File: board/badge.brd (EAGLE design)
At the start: 55.6 x 67.5 mm, 46 parts, among them IC1 STM32F030F4, IC2 UBLOX_MAX, IC3 RFM69HW, IC4 MCP1640, J2 20-0096, J3 SWD_PTH_SHROUD, X1 RADIOMETRIX-MTX2, X2 SMA-142-0701-851/861, X3 091OLED

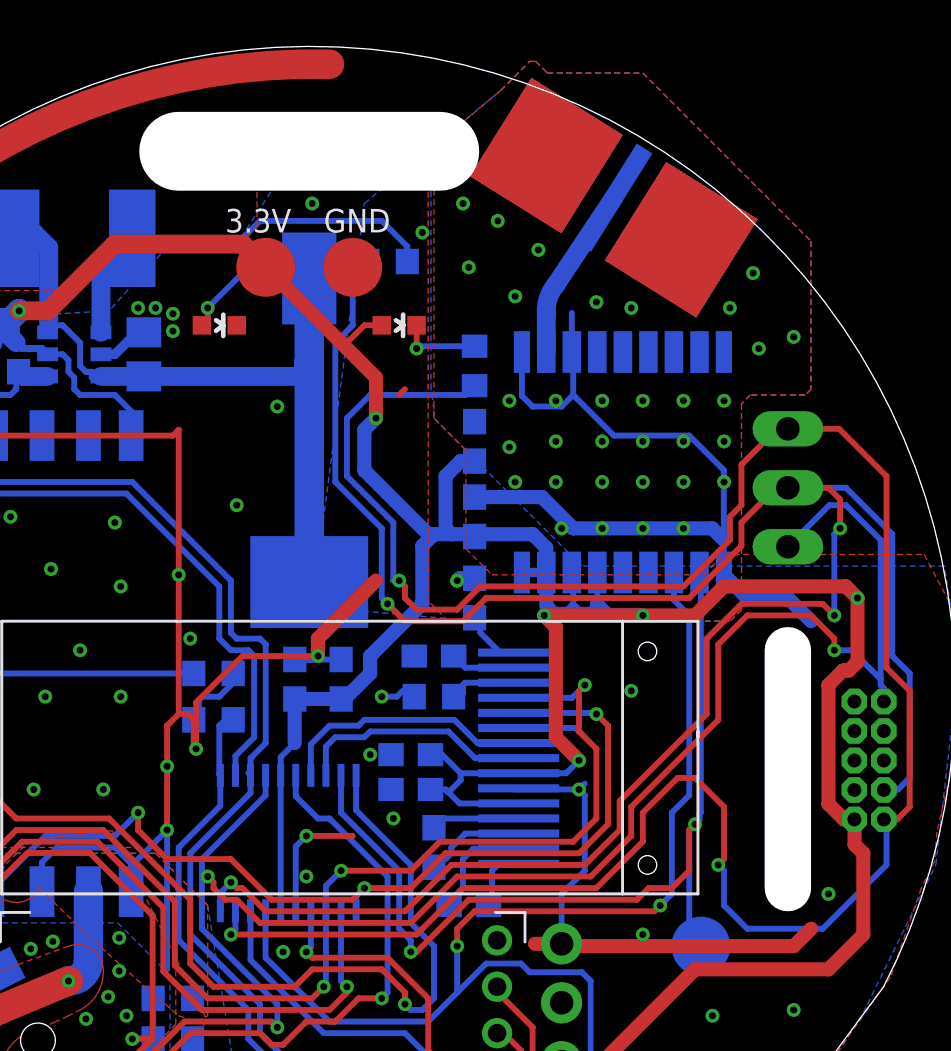
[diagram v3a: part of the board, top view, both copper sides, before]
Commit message: Amended milling layer
Made them dimension layer instead. Confuses the fab by 87.2% less.
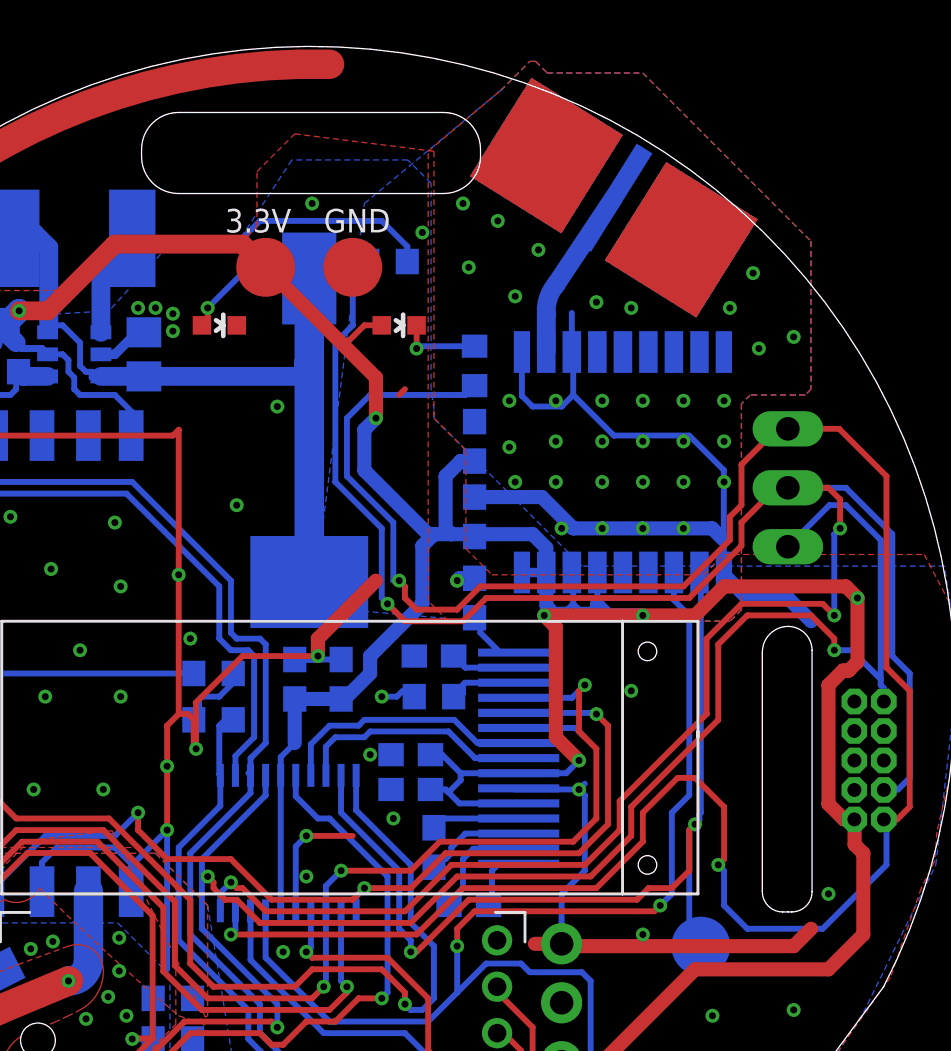
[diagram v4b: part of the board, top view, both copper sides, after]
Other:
- outline, holes or cut-outs redrawn
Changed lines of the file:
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@@
 <setting verticaltext="up"/>
 </settings>
-<grid distance="0.25" unitdist="mm" unit="mm" style="lines" multiple="1" display="no" altdistance="0.125" altunitdist="mm" altunit="mm"/>
+<grid distance="0.079375" unitdist="mm" unit="mm" style="lines" multiple="1" display="yes" altdistance="0.125" altunitdist="mm" altunit="mm"/>
 <layers>
 <layer number="1" name="Top" color="4" fill="1" visible="yes" active="yes"/>
@@
 <layer number="220" name="220bmp" color="21" fill="1" visible="no" active="no"/>
 <layer number="221" name="221bmp" color="22" fill="1" visible="no" active="no"/>
-<layer number="222" name="222bmp" color="23" fill="1" visible="no" active="no"/>
 <layer number="223" name="223bmp" color="24" fill="1" visible="no" active="no"/>
 <layer number="224" name="224bmp" color="25" fill="1" visible="no" active="no"/>
@@
 <text x="48" y="33.5" size="1.016" layer="22" font="vector" ratio="14" rot="SMR90">3.3V only</text>
 <text x="47.5" y="42.75" size="1.016" layer="22" font="vector" ratio="14" rot="MR270">Remove battery</text>
-<wire x1="53.25" y1="55.25" x2="53.25" y2="45" width="2" layer="46"/>
 <text x="54.75" y="60.25" size="1.016" layer="22" font="vector" ratio="13" rot="MR180">RST</text>
 <text x="54.75" y="62.75" size="1.016" layer="22" font="vector" ratio="13" rot="MR180">CLK</text>
@@
 <text x="55" y="66.75" size="1.27" layer="22" font="vector" ratio="13" rot="MR0">SWD</text>
 <text x="58.25" y="45.75" size="1.27" layer="22" font="vector" ratio="13" rot="MR0">SWD</text>
-<wire x1="27" y1="76.75" x2="38.25" y2="76.75" width="3.4" layer="46"/>
 <text x="25" y="22.5" size="1.27" layer="21" font="vector" ratio="13" rot="R90">RESET</text>
 <text x="41.75" y="23" size="1.27" layer="21" font="vector" ratio="13" rot="R90">BOOT</text>
@@
 <wire x1="32.625" y1="12.75" x2="32.625" y2="85.375" width="0" layer="51" style="longdash"/>
 <text x="40" y="17.25" size="1.016" layer="21" font="vector" ratio="14" rot="R56">Rev. A May '14</text>
+<wire x1="26.9875" y1="78.4225" x2="38.4175" y2="78.4225" width="0" layer="20"/>
+<wire x1="38.4175" y1="78.4225" x2="40.005" y2="76.835" width="0" layer="20" curve="-90"/>
+<wire x1="40.005" y1="76.835" x2="40.005" y2="76.5175" width="0" layer="20"/>
+<wire x1="40.005" y1="76.5175" x2="38.4175" y2="74.93" width="0" layer="20" curve="-90"/>
+<wire x1="38.4175" y1="74.93" x2="26.9875" y2="74.93" width="0" layer="20"/>
+<wire x1="26.9875" y1="74.93" x2="25.4" y2="76.5175" width="0" layer="20" curve="-90"/>
+<wire x1="25.4" y1="76.5175" x2="25.4" y2="76.835" width="0" layer="20"/>
+<wire x1="25.4" y1="76.835" x2="26.9875" y2="78.4225" width="0" layer="20" curve="-90"/>
+<wire x1="53.260625" y1="56.276875" x2="54.2925" y2="55.245" width="0" layer="20" curve="-90"/>
+<wire x1="54.2925" y1="55.245" x2="54.2925" y2="44.846875" width="0" layer="20"/>
+<wire x1="54.2925" y1="44.846875" x2="53.419375" y2="43.97375" width="0" layer="20" curve="-90"/>
+<wire x1="53.419375" y1="43.97375" x2="53.260625" y2="43.97375" width="0" layer="20"/>
+<wire x1="53.260625" y1="43.97375" x2="53.0225" y2="43.97375" width="0" layer="20"/>
+<wire x1="53.0225" y1="43.97375" x2="52.149375" y2="44.846875" width="0" layer="20" curve="-90"/>
+<wire x1="52.149375" y1="44.846875" x2="52.149375" y2="55.165625" width="0" layer="20"/>
+<wire x1="52.149375" y1="55.165625" x2="53.260625" y2="56.276875" width="0" layer="20" curve="-90"/>
 </plain>
 <attributes>
@@
 </signal>
 </signals>
-<errors>
-</errors>
 </board>
 </drawing>

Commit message: started rev2
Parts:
- added C13, C14: 1u, rcl:C0603
- added R10: 220k, rcl:R0603
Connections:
- removed net O_RES: IC1.7, X3.9
- new net N$22: C13.2, R10.1, X3.9
- new net N$23: C14.2, J2.4_1, J2.4_2
- new net O_DC: IC1.7, X3.10
- net +3V3: now also R10.2
- net 0V: now also C13.1; no longer X3.10
- net ADC1: now also C14.1; no longer J2.4_1, J2.4_2
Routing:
- net N$22: track 0.00 -> 25.5 mm, vias 0 -> 2
- net O_RES: track 11.1 -> 0.00 mm
- net O_DC: track 0.00 -> 10.9 mm
- net N$9: track 20.6 -> 14.2 mm
- net +3V3: track 217.3 -> 223.1 mm, vias 10 -> 11
- net CS: track 46.0 -> 43.1 mm
- net 0V: track 222.4 -> 220.6 mm, vias 115 -> 121
- net ADC1: track 54.0 -> 52.5 mm
- net N$18: track 43.2 -> 44.5 mm
- net SCK: track 41.0 -> 41.6 mm
- net MOSI: track 54.0 -> 54.6 mm
- net TX: track 13.7 -> 14.3 mm
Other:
- outline, holes or cut-outs redrawn

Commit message: rev2 almost done
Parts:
- added R11: 10k, rcl:R0603
- moved C14 1.67 mm to (26.8, 35.0)
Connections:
- new net N$24: C14.1, R11.2
- net ADC1: now also R11.1; no longer C14.1
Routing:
- net 0V: track 220.6 -> 191.6 mm, vias 121 -> 131
- net N$23: track 0.00 -> 26.6 mm, vias 0 -> 2
- net ADC1: track 52.5 -> 29.0 mm, vias 5 -> 2
- net N$9: track 14.2 -> 21.8 mm, vias 0 -> 2
- net N$19: track 14.2 -> 11.2 mm
- net N$18: track 44.5 -> 42.1 mm
- net N$24: track 0.00 -> 1.75 mm
- net N$8: track 52.5 -> 51.5 mm
- net TX_EN: track 62.1 -> 62.6 mm
- net +3V3: track 223.1 -> 223.6 mm

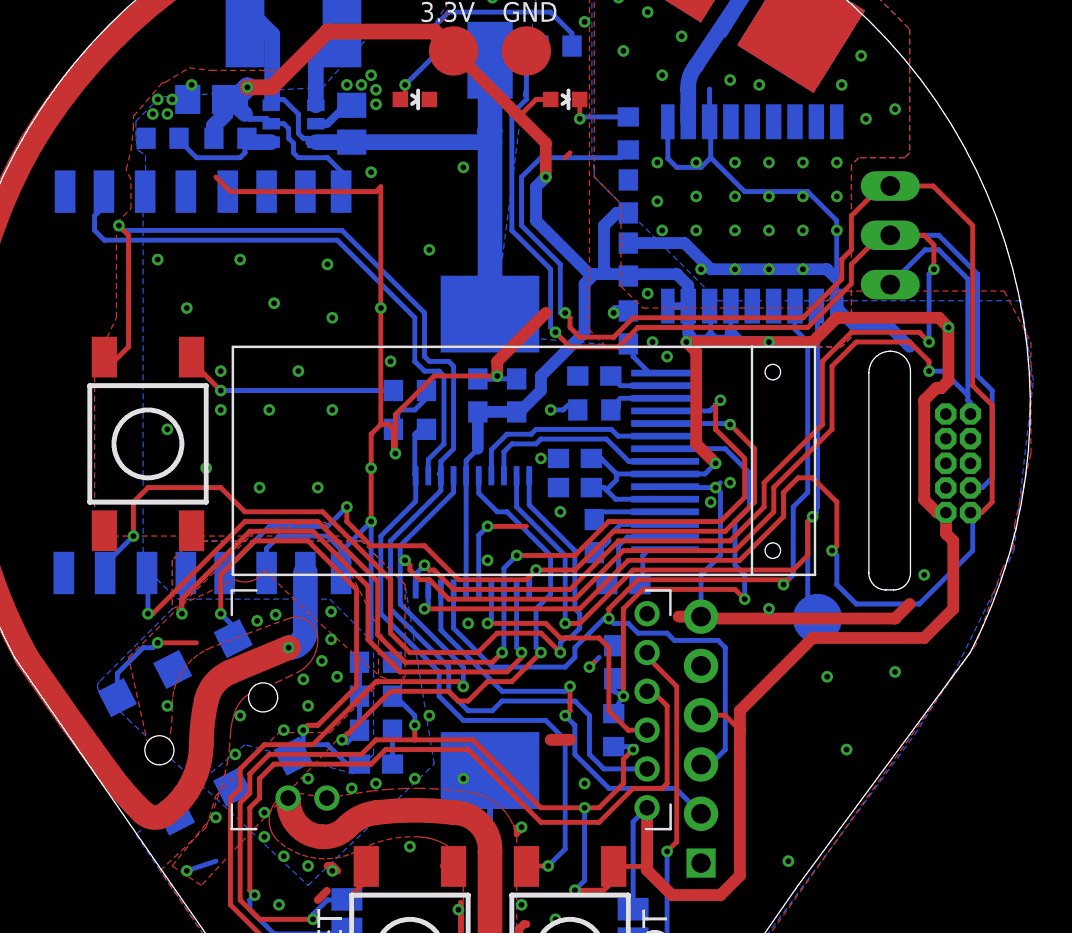
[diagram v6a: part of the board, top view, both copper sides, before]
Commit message: switching tx/rx on ftdi
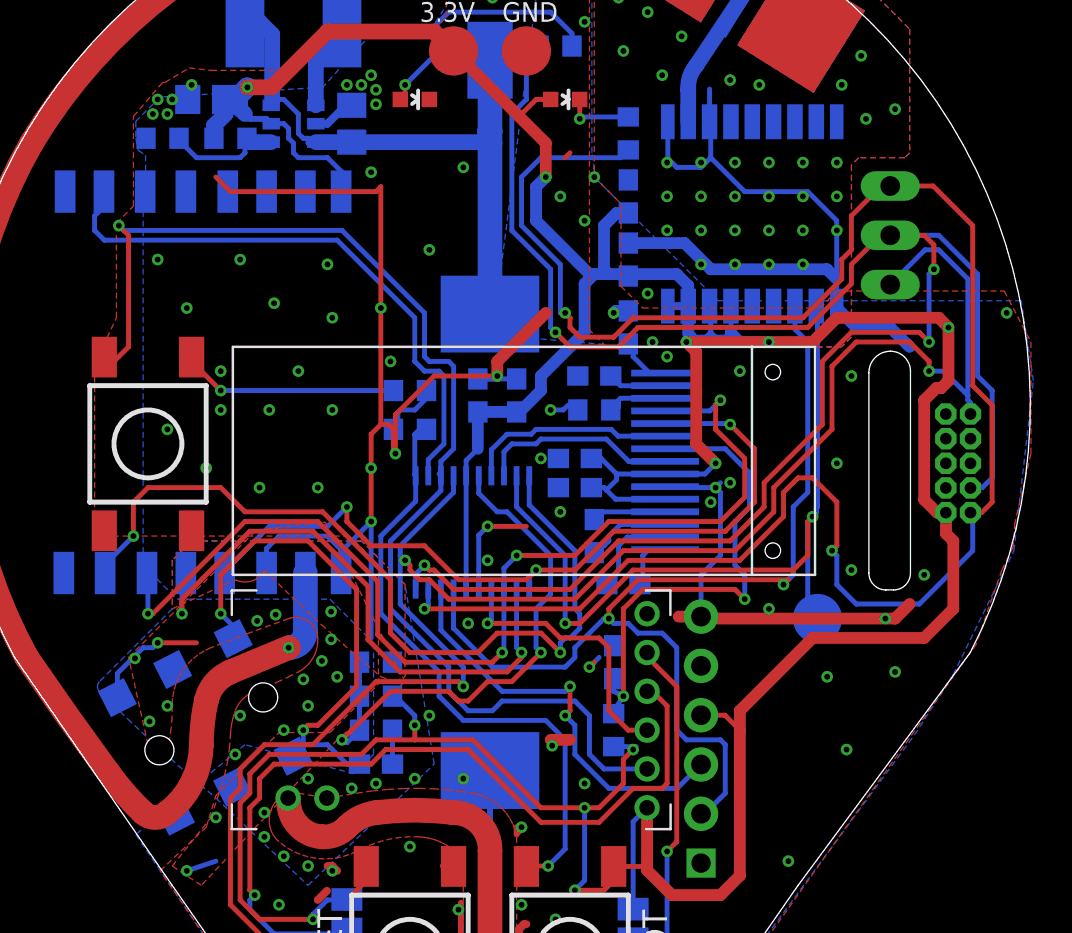
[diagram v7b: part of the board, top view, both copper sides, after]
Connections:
- net N$8: now also JP1.P$2; no longer JP1.P$3
- net N$9: now also JP1.P$3; no longer JP1.P$2
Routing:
- net N$8: track 51.5 -> 53.4 mm
- net 0V: vias 131 -> 143
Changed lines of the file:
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@@
 <setting verticaltext="up"/>
 </settings>
-<grid distance="9.84251969" unitdist="mil" unit="mil" style="lines" multiple="1" display="yes" altdistance="0.125" altunitdist="mm" altunit="mm"/>
+<grid distance="0.25" unitdist="mm" unit="mm" style="lines" multiple="1" display="yes" altdistance="0.125" altunitdist="mm" altunit="mm"/>
 <layers>
 <layer number="1" name="Top" color="4" fill="1" visible="yes" active="yes"/>
@@
 <vertex x="13.375" y="58"/>
 <vertex x="13.375" y="62.875"/>
-<vertex x="14.125" y="63.625"/>
-<vertex x="14.125" y="65.125"/>
-<vertex x="13.875" y="65.625"/>
-<vertex x="14.125" y="66.625"/>
-<vertex x="14.25" y="67.75"/>
+<vertex x="14.25" y="63.75"/>
 <vertex x="14.25" y="68.375"/>
 <vertex x="15.75" y="70.125"/>
@@
 <vertex x="40.99" y="17.72625"/>
 </polygon>
-<via x="48.75" y="60.5" extent="1-16" drill="0.3"/>
+<via x="48.75" y="60.75" extent="1-16" drill="0.3"/>
 <via x="48.75" y="64.25" extent="1-16" drill="0.3"/>
-<via x="47" y="60.5" extent="1-16" drill="0.3"/>
+<via x="47" y="60.75" extent="1-16" drill="0.3"/>
 <via x="47" y="62.5" extent="1-16" drill="0.3"/>
 <via x="47" y="64.25" extent="1-16" drill="0.3"/>
 <via x="47" y="66" extent="1-16" drill="0.3"/>
-<via x="45.25" y="60.5" extent="1-16" drill="0.3"/>
+<via x="45.25" y="60.75" extent="1-16" drill="0.3"/>
 <via x="48.75" y="66" extent="1-16" drill="0.3"/>
 <via x="50.5" y="66" extent="1-16" drill="0.3"/>
@@
 <via x="45.25" y="64.25" extent="1-16" drill="0.3"/>
 <via x="45.25" y="66" extent="1-16" drill="0.3"/>
-<via x="43.25" y="62.5" extent="1-16" drill="0.3"/>
-<via x="43.25" y="64.25" extent="1-16" drill="0.3"/>
-<via x="43.25" y="66" extent="1-16" drill="0.3"/>
-<via x="41.25" y="66" extent="1-16" drill="0.3"/>
-<via x="41.25" y="64" extent="1-16" drill="0.3"/>
-<via x="41.5" y="62.5" extent="1-16" drill="0.3"/>
-<via x="43.5" y="60.5" extent="1-16" drill="0.3"/>
+<via x="43.5" y="62.5" extent="1-16" drill="0.3"/>
+<via x="43.5" y="64.25" extent="1-16" drill="0.3"/>
+<via x="43.5" y="66" extent="1-16" drill="0.3"/>
+<via x="41.75" y="66" extent="1-16" drill="0.3"/>
+<via x="41.75" y="64.25" extent="1-16" drill="0.3"/>
+<via x="41.75" y="62.5" extent="1-16" drill="0.3"/>
+<via x="43.5" y="60.75" extent="1-16" drill="0.3"/>
 <via x="51.75" y="71.5" extent="1-16" drill="0.3"/>
 <via x="50.75" y="70" extent="1-16" drill="0.3"/>
@@
 <via x="19.5" y="25.75" extent="1-16" drill="0.3"/>
 <via x="21" y="32.5" extent="1-16" drill="0.3"/>
+<via x="14.32875" y="40.44875" extent="1-16" drill="0.3"/>
+<via x="15.07875" y="37.19875" extent="1-16" drill="0.3"/>
+<via x="35.82875" y="35.94875" extent="1-16" drill="0.3"/>
+<via x="45.5" y="55.25" extent="1-16" drill="0.3"/>
+<via x="51.25" y="55" extent="1-16" drill="0.3"/>
+<via x="50.5" y="50.5" extent="1-16" drill="0.3"/>
+<via x="51.25" y="45" extent="1-16" drill="0.3"/>
+<via x="53" y="42.5" extent="1-16" drill="0.3"/>
+<via x="59.25" y="58.25" extent="1-16" drill="0.3"/>
+<via x="38" y="65.25" extent="1-16" drill="0.3"/>
+<via x="37.5" y="63" extent="1-16" drill="0.3"/>
+<via x="36.25" y="64.25" extent="1-16" drill="0.3"/>
 </signal>
 <signal name="N$8">
-<contactref element="JP1" pad="P$3"/>
 <contactref element="IC1" pad="17"/>
 <contactref element="IC2" pad="3_RXD1"/>
@@
 <wire x1="38.75" y1="43" x2="38.75" y2="42.5" width="0.254" layer="1"/>
 <via x="38.75" y="42.5" extent="1-16" drill="0.3"/>
-<wire x1="43.5" y1="34.98" x2="43.98" y2="34.98" width="0.254" layer="16"/>
-<wire x1="43.98" y1="34.98" x2="44.75" y2="35.75" width="0.254" layer="16"/>
-<wire x1="44.75" y1="35.75" x2="44.75" y2="41" width="0.254" layer="16"/>
-<wire x1="44.75" y1="41" x2="44.375" y2="41.375" width="0.254" layer="16"/>
-<wire x1="44.375" y1="41.375" x2="42.125" y2="41.375" width="0.254" layer="16"/>
-<wire x1="42.125" y1="41.375" x2="41.75" y2="41.75" width="0.254" layer="16"/>
-<wire x1="41.75" y1="41.75" x2="40.25" y2="41.75" width="0.254" layer="16"/>
+<wire x1="41.5" y1="41.75" x2="40.25" y2="41.75" width="0.254" layer="16"/>
 <wire x1="37" y1="41" x2="38.5" y2="42.5" width="0.254" layer="16"/>
 <wire x1="40.25" y1="41.75" x2="39.75" y2="42.25" width="0.254" layer="16"/>
@@
 <wire x1="36.5" y1="40" x2="32.75" y2="40" width="0.254" layer="16"/>
 <wire x1="32.75" y1="40" x2="30.745" y2="42.005" width="0.254" layer="16"/>
+<contactref element="JP1" pad="P$2"/>
+<wire x1="43.5" y1="32.44" x2="43.69" y2="32.44" width="0.254" layer="16"/>
+<wire x1="43.69" y1="32.44" x2="44.75" y2="33.5" width="0.254" layer="16"/>
+<wire x1="44.75" y1="33.5" x2="44.75" y2="36" width="0.254" layer="16"/>
+<wire x1="44.75" y1="36" x2="44.5" y2="36.25" width="0.254" layer="16"/>
+<wire x1="44.5" y1="36.25" x2="42.75" y2="36.25" width="0.254" layer="16"/>
+<wire x1="42.75" y1="36.25" x2="42.25" y2="36.75" width="0.254" layer="16"/>
+<wire x1="42.25" y1="36.75" x2="42.25" y2="41" width="0.254" layer="16"/>
+<wire x1="42.25" y1="41" x2="41.5" y2="41.75" width="0.254" layer="16"/>
 </signal>
 <signal name="N$9">
-<contactref element="JP1" pad="P$2"/>
 <contactref element="IC1" pad="18"/>
 <wire x1="30.095" y1="44.0222" x2="30.095" y2="41.905" width="0.254" layer="16"/>
 <via x="36.75" y="39" extent="1-16" drill="0.3"/>
-<wire x1="42.19" y1="33.75" x2="43.5" y2="32.44" width="0.254" layer="16"/>
 <wire x1="36.75" y1="39" x2="36.75" y2="37.75" width="0.254" layer="1"/>
 <wire x1="36.75" y1="37.75" x2="36.5" y2="37.5" width="0.254" layer="1"/>
@@
 <wire x1="33.25" y1="38.75" x2="30.095" y2="41.905" width="0.254" layer="16"/>
 <wire x1="37" y1="35.5" x2="38.75" y2="33.75" width="0.254" layer="16"/>
-<wire x1="38.75" y1="33.75" x2="42.19" y2="33.75" width="0.254" layer="16"/>
+<wire x1="38.75" y1="33.75" x2="42.27" y2="33.75" width="0.254" layer="16"/>
+<contactref element="JP1" pad="P$3"/>
+<wire x1="42.27" y1="33.75" x2="43.5" y2="34.98" width="0.254" layer="16"/>
 </signal>
 <signal name="N$10">
